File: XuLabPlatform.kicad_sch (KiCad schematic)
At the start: 9 parts, among them J10 Servo7, J11 Servo8, J12 Thruster SGN, J4 Servo1, J5 Servo2, J6 Servo3, J7 Servo4, J8 Servo5, J9 Servo6

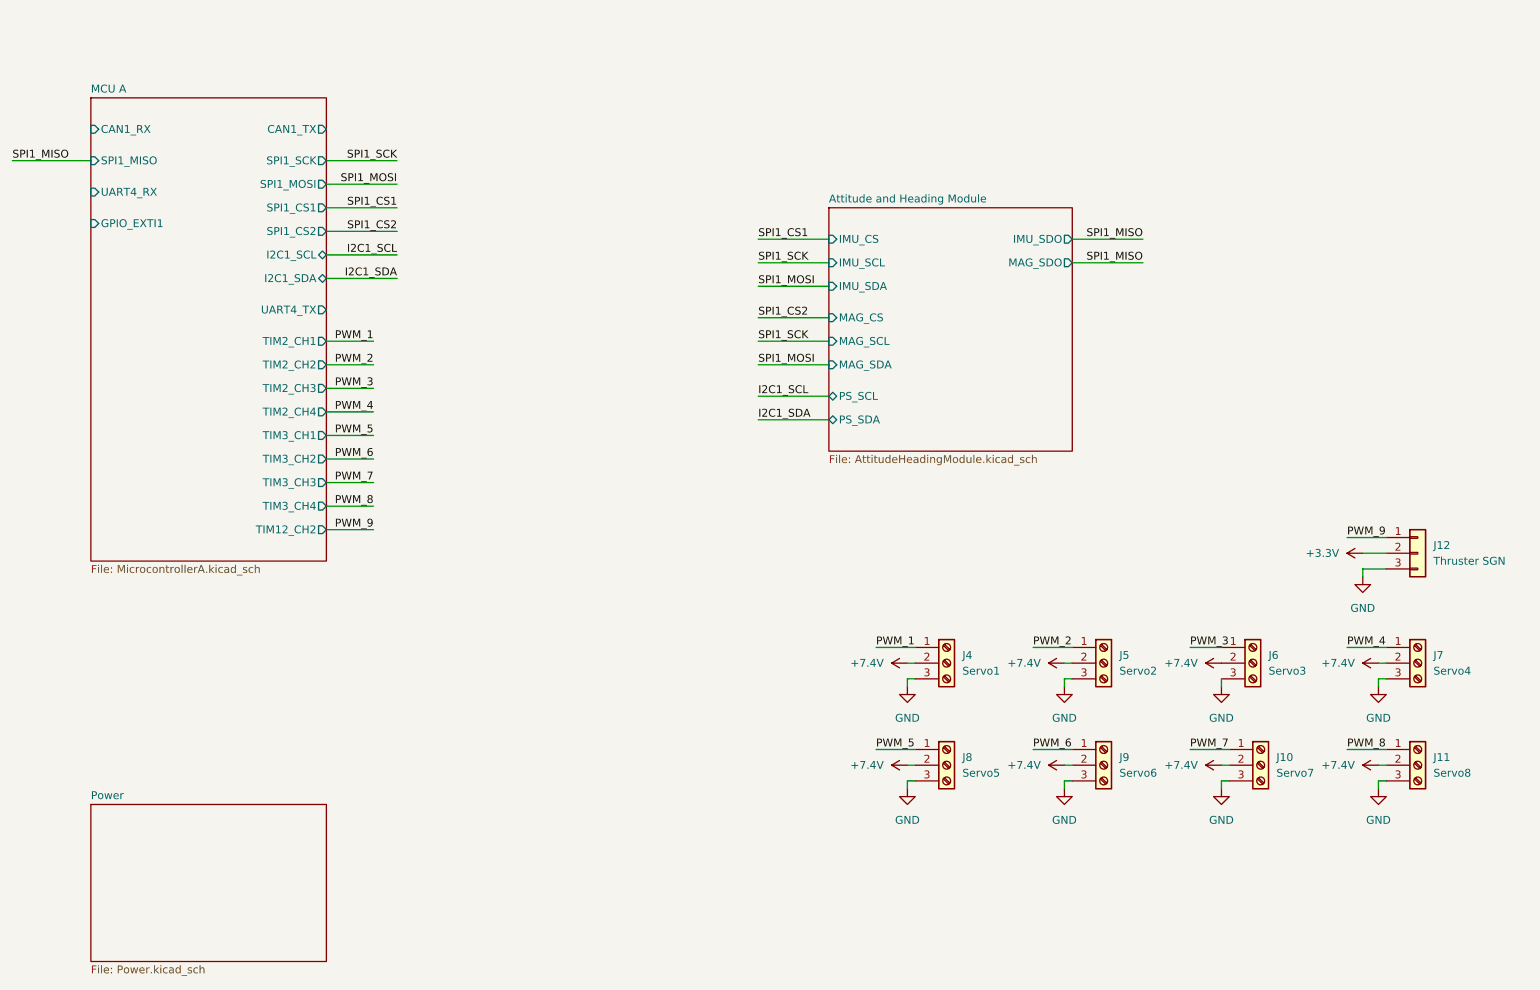
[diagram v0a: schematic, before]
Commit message: Add breakout sockets for microcontroller IO lines
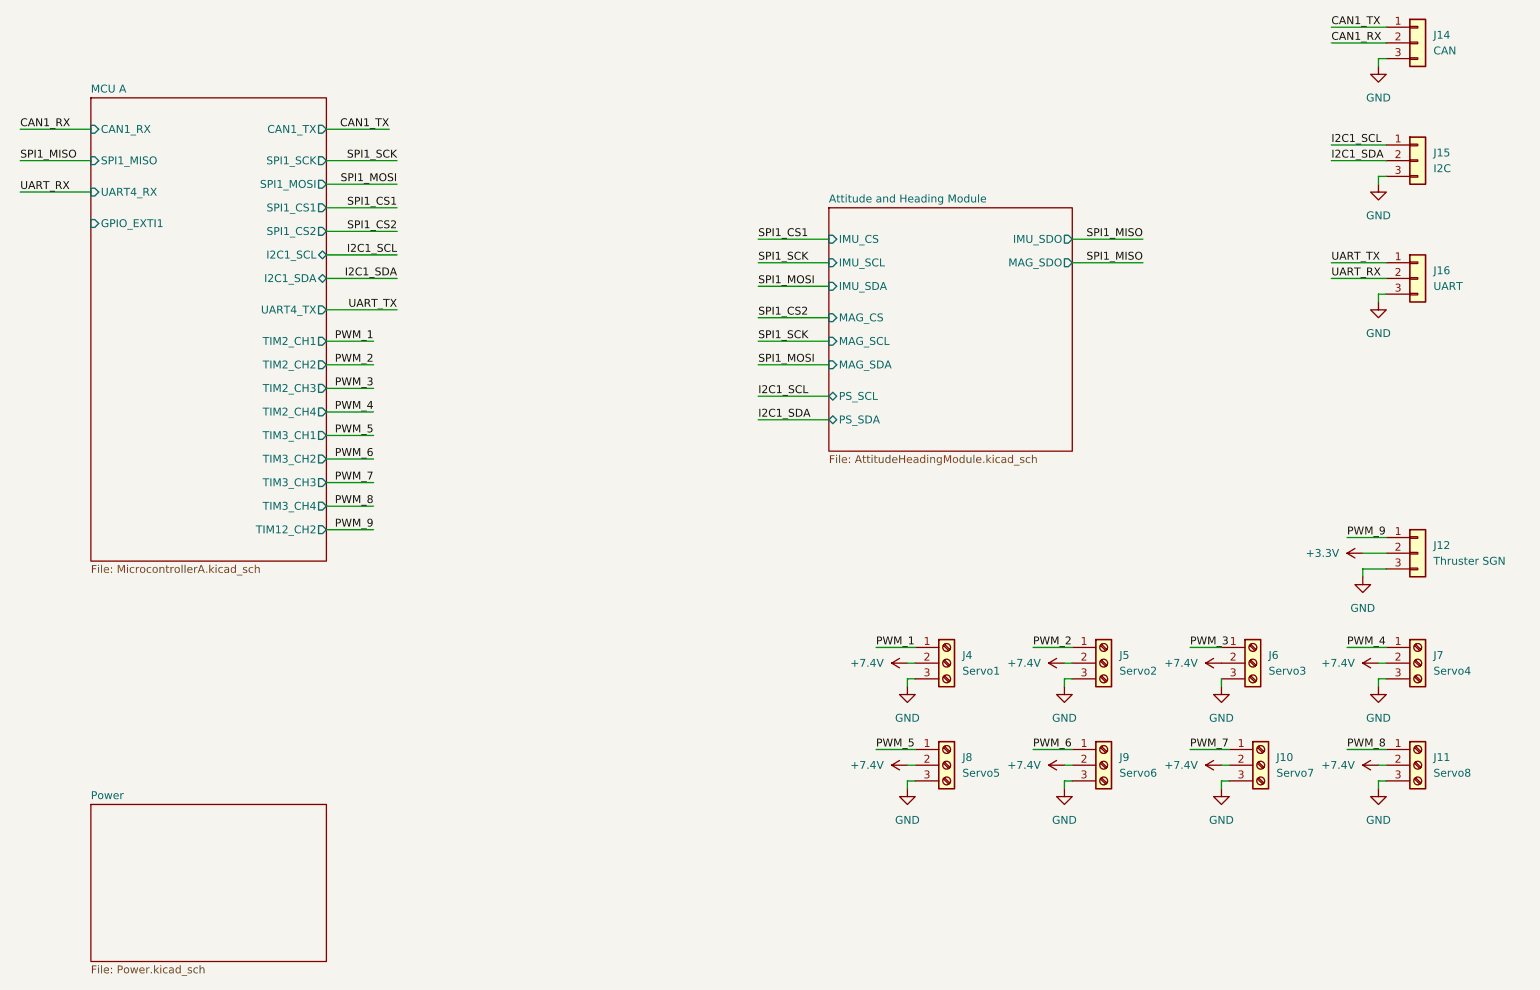
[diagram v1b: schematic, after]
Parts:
- added J14: CAN, Connector_PinSocket_2.00mm:PinSocket_1x03_P2.00mm_Vertical, symbol Connector_Generic:Conn_01x03
- added J15: I2C, Connector_PinSocket_2.00mm:PinSocket_1x03_P2.00mm_Vertical, symbol Connector_Generic:Conn_01x03
- added J16: UART, Connector_PinSocket_2.00mm:PinSocket_1x03_P2.00mm_Vertical, symbol Connector_Generic:Conn_01x03
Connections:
- net GND: now also J14.3 (Pin_3), J15.3 (Pin_3), J16.3 (Pin_3)
- net I2C1_SCL: now also J15.1 (Pin_1)
- net I2C1_SDA: now also J15.2 (Pin_2)
- new net CAN1_RX: J14.2 (Pin_2)
- new net CAN1_TX: J14.1 (Pin_1)
- new net UART_RX: J16.2 (Pin_2)
- new net UART_TX: J16.1 (Pin_1)

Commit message: Add rest of connections
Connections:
- net GND: now also J10.1 (Pin_1), J11.1 (Pin_1), J12.1 (Pin_1), J8.1 (Pin_1), J9.1 (Pin_1); no longer J10.3 (Pin_3), J11.3 (Pin_3), J12.3 (Pin_3), J8.3 (Pin_3), J9.3 (Pin_3)
- net I2C1_SCL: now also J15.2 (Pin_2); no longer J15.1 (Pin_1)
- net I2C1_SDA: now also J15.1 (Pin_1); no longer J15.2 (Pin_2)
- net PWM_5: now also J8.3 (Pin_3); no longer J8.1 (Pin_1)
- net PWM_6: now also J9.3 (Pin_3); no longer J9.1 (Pin_1)
- net PWM_7: now also J10.3 (Pin_3); no longer J10.1 (Pin_1)
- net PWM_8: now also J11.3 (Pin_3); no longer J11.1 (Pin_1)
- net PWM_9: now also J12.3 (Pin_3); no longer J12.1 (Pin_1)
- net UART_RX: now also J16.1 (Pin_1); no longer J16.2 (Pin_2)
- net UART_TX: now also J16.2 (Pin_2); no longer J16.1 (Pin_1)
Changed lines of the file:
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@@
+		)
+	)
+	(label "I2C1_SCL"
+		(at 251.46 48.26 0)
+		(effects
+			(font
+				(size 1.27 1.27)
+			)
+			(justify left bottom)
 		)
 	)
@@
 		)
 	)
-	(label "UART_RX"
-		(at 251.46 67.31 0)
-		(effects
-			(font
-				(size 1.27 1.27)
-			)
-			(justify left bottom)
-		)
-	)
 	(label "SPI1_SCK"
 		(at 158.75 77.47 0)
@@
 		)
 	)
+	(label "UART_RX"
+		(at 251.46 64.77 0)
+		(effects
+			(font
+				(size 1.27 1.27)
+			)
+			(justify left bottom)
+		)
+	)
 	(label "PWM_5"
 		(at 96.52 92.71 180)
@@
 		)
 	)
-	(label "I2C1_SCL"
-		(at 251.46 45.72 0)
-		(effects
-			(font
-				(size 1.27 1.27)
-			)
-			(justify left bottom)
-		)
-	)
 	(label "SPI1_CS1"
 		(at 158.75 60.96 0)
@@
 		)
 	)
+	(label "I2C1_SDA"
+		(at 251.46 45.72 0)
+		(effects
+			(font
+				(size 1.27 1.27)
+			)
+			(justify left bottom)
+		)
+	)
 	(label "PWM_4"
 		(at 96.52 88.9 180)
@@
 	)
 	(label "I2C1_SDA"
-		(at 251.46 48.26 0)
-		(effects
-			(font
-				(size 1.27 1.27)
-			)
-			(justify left bottom)
-		)
-	)
-	(label "I2C1_SDA"
 		(at 100.33 67.31 180)
 		(effects
@@
 		)
 	)
+	(label "UART_TX"
+		(at 251.46 67.31 0)
+		(effects
+			(font
+				(size 1.27 1.27)
+			)
+			(justify left bottom)
+		)
+	)
 	(label "SPI1_CS2"
 		(at 158.75 73.66 0)
@@
 		)
 	)
-	(label "UART_TX"
-		(at 251.46 64.77 0)
-		(effects
-			(font
-				(size 1.27 1.27)
-			)
-			(justify left bottom)
-		)
-	)
 	(label "PWM_5"
 		(at 177.8 143.51 0)
@@
 		(lib_id "Connector:Screw_Terminal_01x03")
 		(at 214.63 146.05 0)
-		(unit 1)
-		(exclude_from_sim no)
-		(in_bom yes)
-		(on_board yes)
-		(dnp no)
-		(fields_autoplaced yes)
+		(mirror x)
+		(unit 1)
+		(exclude_from_sim no)
+		(in_bom yes)
+		(on_board yes)
+		(dnp no)
 		(property "Reference" "J9"
-			(at 217.17 144.7799 0)
+			(at 217.17 147.3201 0)
 			(effects
 				(font
@@
 		)
 		(property "Value" "Servo6"
-			(at 217.17 147.3199 0)
+			(at 217.17 144.7801 0)
 			(effects
 				(font
@@
 		(lib_id "Connector:Screw_Terminal_01x03")
 		(at 189.23 146.05 0)
-		(unit 1)
-		(exclude_from_sim no)
-		(in_bom yes)
-		(on_board yes)
-		(dnp no)
-		(fields_autoplaced yes)
+		(mirror x)
+		(unit 1)
+		(exclude_from_sim no)
+		(in_bom yes)
+		(on_board yes)
+		(dnp no)
 		(property "Reference" "J8"
-			(at 191.77 144.7799 0)
+			(at 191.77 147.3201 0)
 			(effects
 				(font
@@
 		)
 		(property "Value" "Servo5"
-			(at 191.77 147.3199 0)
+			(at 191.77 144.7801 0)
 			(effects
 				(font
@@
 		(lib_id "Connector:Screw_Terminal_01x03")
 		(at 240.03 146.05 0)
-		(unit 1)
-		(exclude_from_sim no)
-		(in_bom yes)
-		(on_board yes)
-		(dnp no)
-		(fields_autoplaced yes)
+		(mirror x)
+		(unit 1)
+		(exclude_from_sim no)
+		(in_bom yes)
+		(on_board yes)
+		(dnp no)
 		(property "Reference" "J10"
-			(at 242.57 144.7799 0)
+			(at 242.57 147.3201 0)
 			(effects
 				(font
@@
 		)
 		(property "Value" "Servo7"
-			(at 242.57 147.3199 0)
+			(at 242.57 144.7801 0)
 			(effects
 				(font
@@
 		(lib_id "Connector_Generic:Conn_01x03")
 		(at 265.43 111.76 0)
-		(unit 1)
-		(exclude_from_sim no)
-		(in_bom yes)
-		(on_board yes)
-		(dnp no)
-		(fields_autoplaced yes)
+		(mirror x)
+		(unit 1)
+		(exclude_from_sim no)
+		(in_bom yes)
+		(on_board yes)
+		(dnp no)
 		(property "Reference" "J12"
-			(at 267.97 110.4899 0)
+			(at 267.97 113.0301 0)
 			(effects
 				(font
@@
 		)
 		(property "Value" "Thruster SGN"
-			(at 267.97 113.0299 0)
+			(at 267.97 110.4901 0)
 			(effects
 				(font
@@
 		(lib_id "Connector:Screw_Terminal_01x03")
 		(at 265.43 146.05 0)
-		(unit 1)
-		(exclude_from_sim no)
-		(in_bom yes)
-		(on_board yes)
-		(dnp no)
-		(fields_autoplaced yes)
+		(mirror x)
+		(unit 1)
+		(exclude_from_sim no)
+		(in_bom yes)
+		(on_board yes)
+		(dnp no)
 		(property "Reference" "J11"
-			(at 267.97 144.7799 0)
+			(at 267.97 147.3201 0)
 			(effects
 				(font
@@
 		)
 		(property "Value" "Servo8"
-			(at 267.97 147.3199 0)
-			(effects
-				(font
+			(at 267.97 144.7801 0)
+			(effects
+				(font

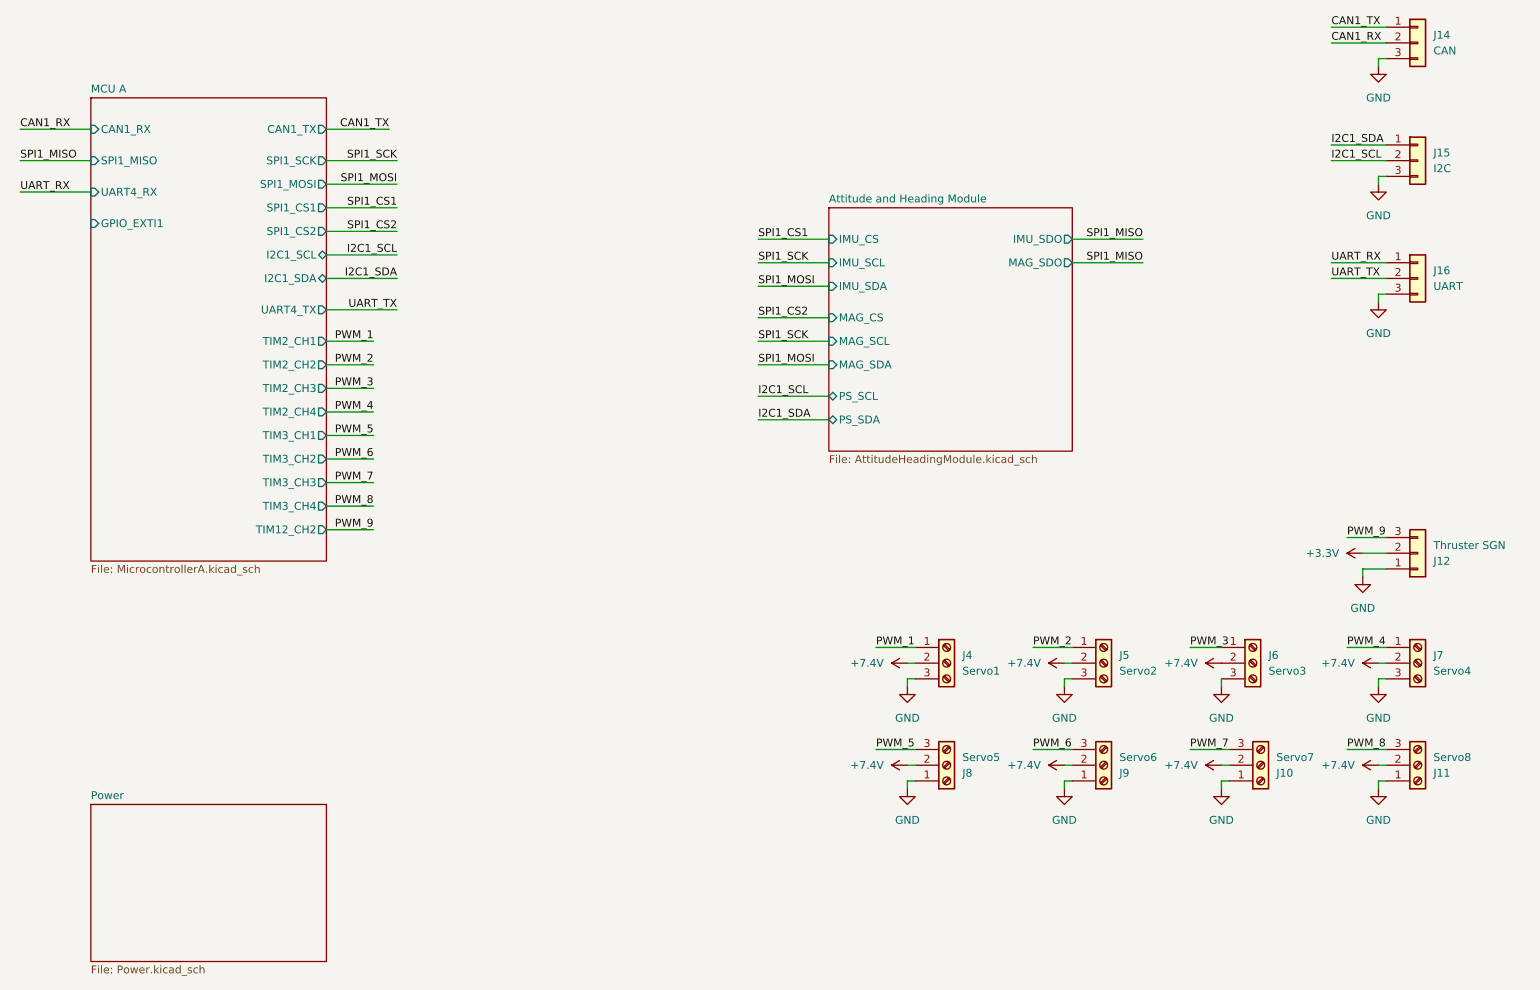
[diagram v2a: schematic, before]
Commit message: Change IMU to BMI088
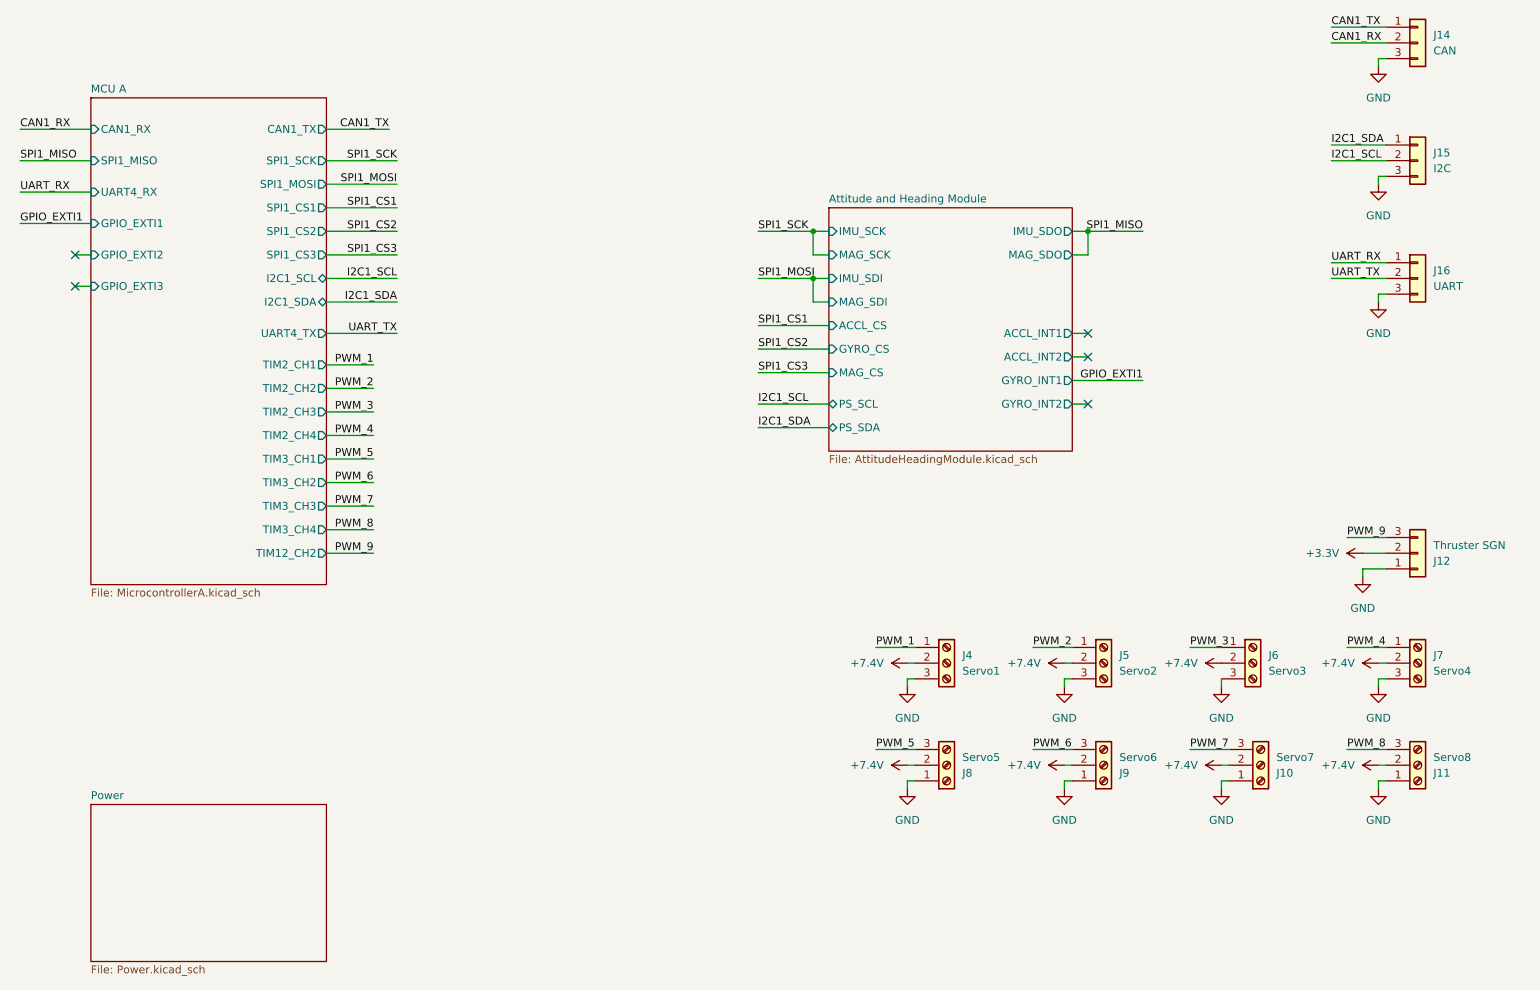
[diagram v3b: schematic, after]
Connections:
- no-connect marks 0 -> 5
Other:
- sheet Attitude and Heading Module ports: added ACCL_CS, ACCL_INT1, ACCL_INT2, GYRO_CS, GYRO_INT1, GYRO_INT2, IMU_SCK, IMU_SDI, MAG_SCK, MAG_SDI; removed IMU_CS, IMU_SCL, IMU_SDA, MAG_SCL, MAG_SDA
- sheet MCU A ports: added GPIO_EXTI2, GPIO_EXTI3, SPI1_CS3; removed none
